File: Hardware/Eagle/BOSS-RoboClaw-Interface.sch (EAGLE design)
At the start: 10 parts, among them IC1 ISO7221AQDRQ1, J1 MOLEX 22112024, J2 MOLEX 22122034, J3 Amphenol 75869-130LF, J5 SAMTEC ESQ-110-33-T-D, J6 SAMTEC-ESQ-105-33-T-S, X1 Amphenol L77SDAH15SOL2RM8C309

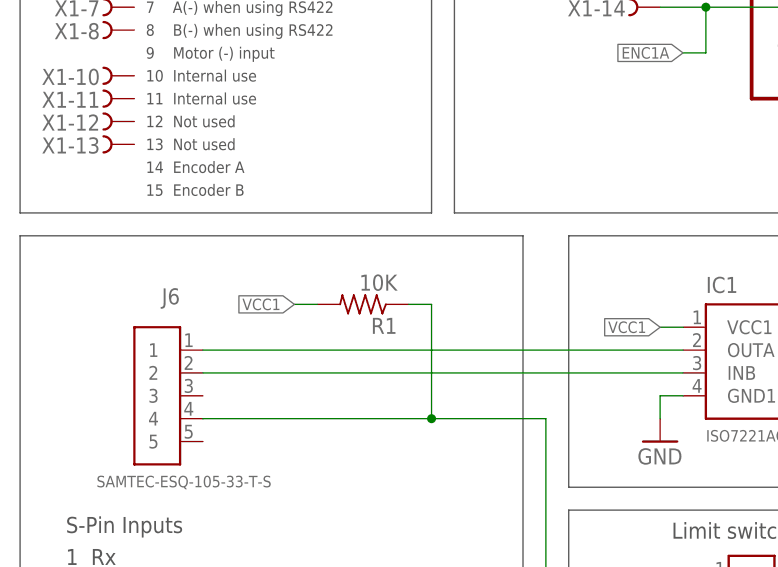
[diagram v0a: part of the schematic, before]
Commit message: Changed limit switch pullup to 4.7K
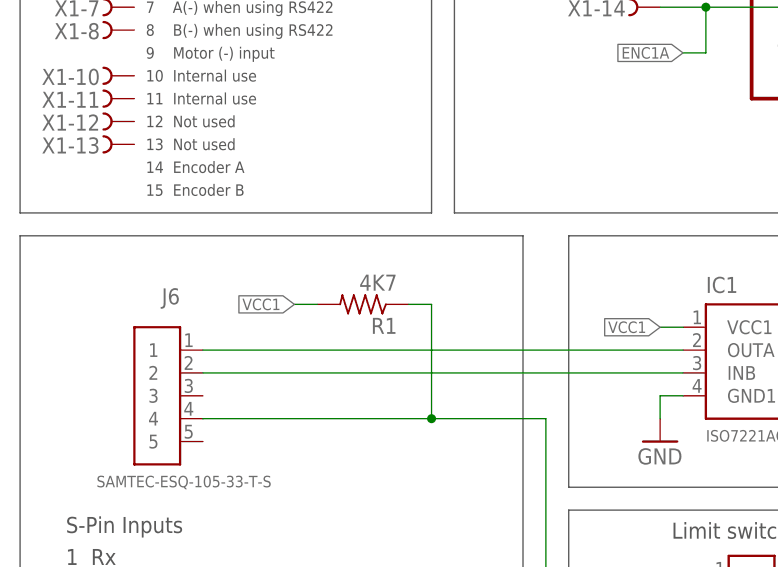
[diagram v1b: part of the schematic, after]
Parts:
- R1: value 10K -> 4K7
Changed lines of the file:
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@@
 <setting verticaltext="up"/>
 </settings>
-<grid distance="0.1" unitdist="inch" unit="inch" style="lines" multiple="1" display="yes" altdistance="0.01" altunitdist="inch" altunit="inch"/>
+<grid distance="0.1" unitdist="inch" unit="inch" style="lines" multiple="1" display="no" altdistance="0.01" altunitdist="inch" altunit="inch"/>
 <layers>
 <layer number="1" name="Top" color="4" fill="1" visible="no" active="no"/>
@@
 <part name="J6" library="AUmlib" library_urn="urn:adsk.eagle:library:9166017" deviceset="PINHD-1X5-ESQ-105-33-T-S" device="" package3d_urn="urn:adsk.eagle:package:24929591/4" value="SAMTEC-ESQ-105-33-T-S"/>
 <part name="J5" library="AUmlib" library_urn="urn:adsk.eagle:library:9166017" deviceset="PINHD-2X10-ESQ-110-33-T-D" device="SAMTEC" package3d_urn="urn:adsk.eagle:package:24929474/2" value="SAMTEC ESQ-110-33-T-D"/>
-<part name="R1" library="AUmlib" library_urn="urn:adsk.eagle:library:9166017" deviceset="R-US_" device="R0805" package3d_urn="urn:adsk.eagle:package:4021199/4" value="10K"/>
+<part name="R1" library="AUmlib" library_urn="urn:adsk.eagle:library:9166017" deviceset="R-US_" device="R0805" package3d_urn="urn:adsk.eagle:package:4021199/4" value="4K7"/>
 </parts>
 <sheets>

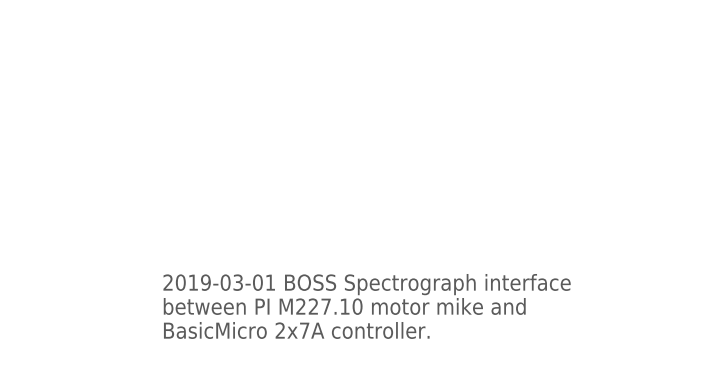
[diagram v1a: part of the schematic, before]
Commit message: Created a motor breakout board
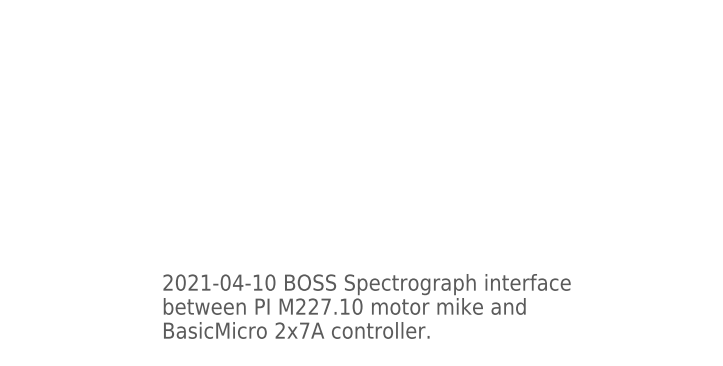
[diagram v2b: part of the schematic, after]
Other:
- note added: "2021-04-10 BOSS Spectrograph interface between PI M227.10 motor mike and BasicMicro 2x7A controller."
- note removed: "2019-03-01 BOSS Spectrograph interface between PI M227.10 motor mike and BasicMicro 2x7A controller."
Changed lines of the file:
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@@
 <wire x1="116.84" y1="129.54" x2="195.58" y2="129.54" width="0.1524" layer="97"/>
 <text x="172.72" y="170.18" size="1.778" layer="97" distance="100">Encoder Inputs</text>
-<text x="180.34" y="25.4" size="1.778" layer="97">2019-03-01 BOSS Spectrograph interface
+<text x="180.34" y="25.4" size="1.778" layer="97">2021-04-10 BOSS Spectrograph interface
 between PI M227.10 motor mike and
 BasicMicro 2x7A controller.</text>

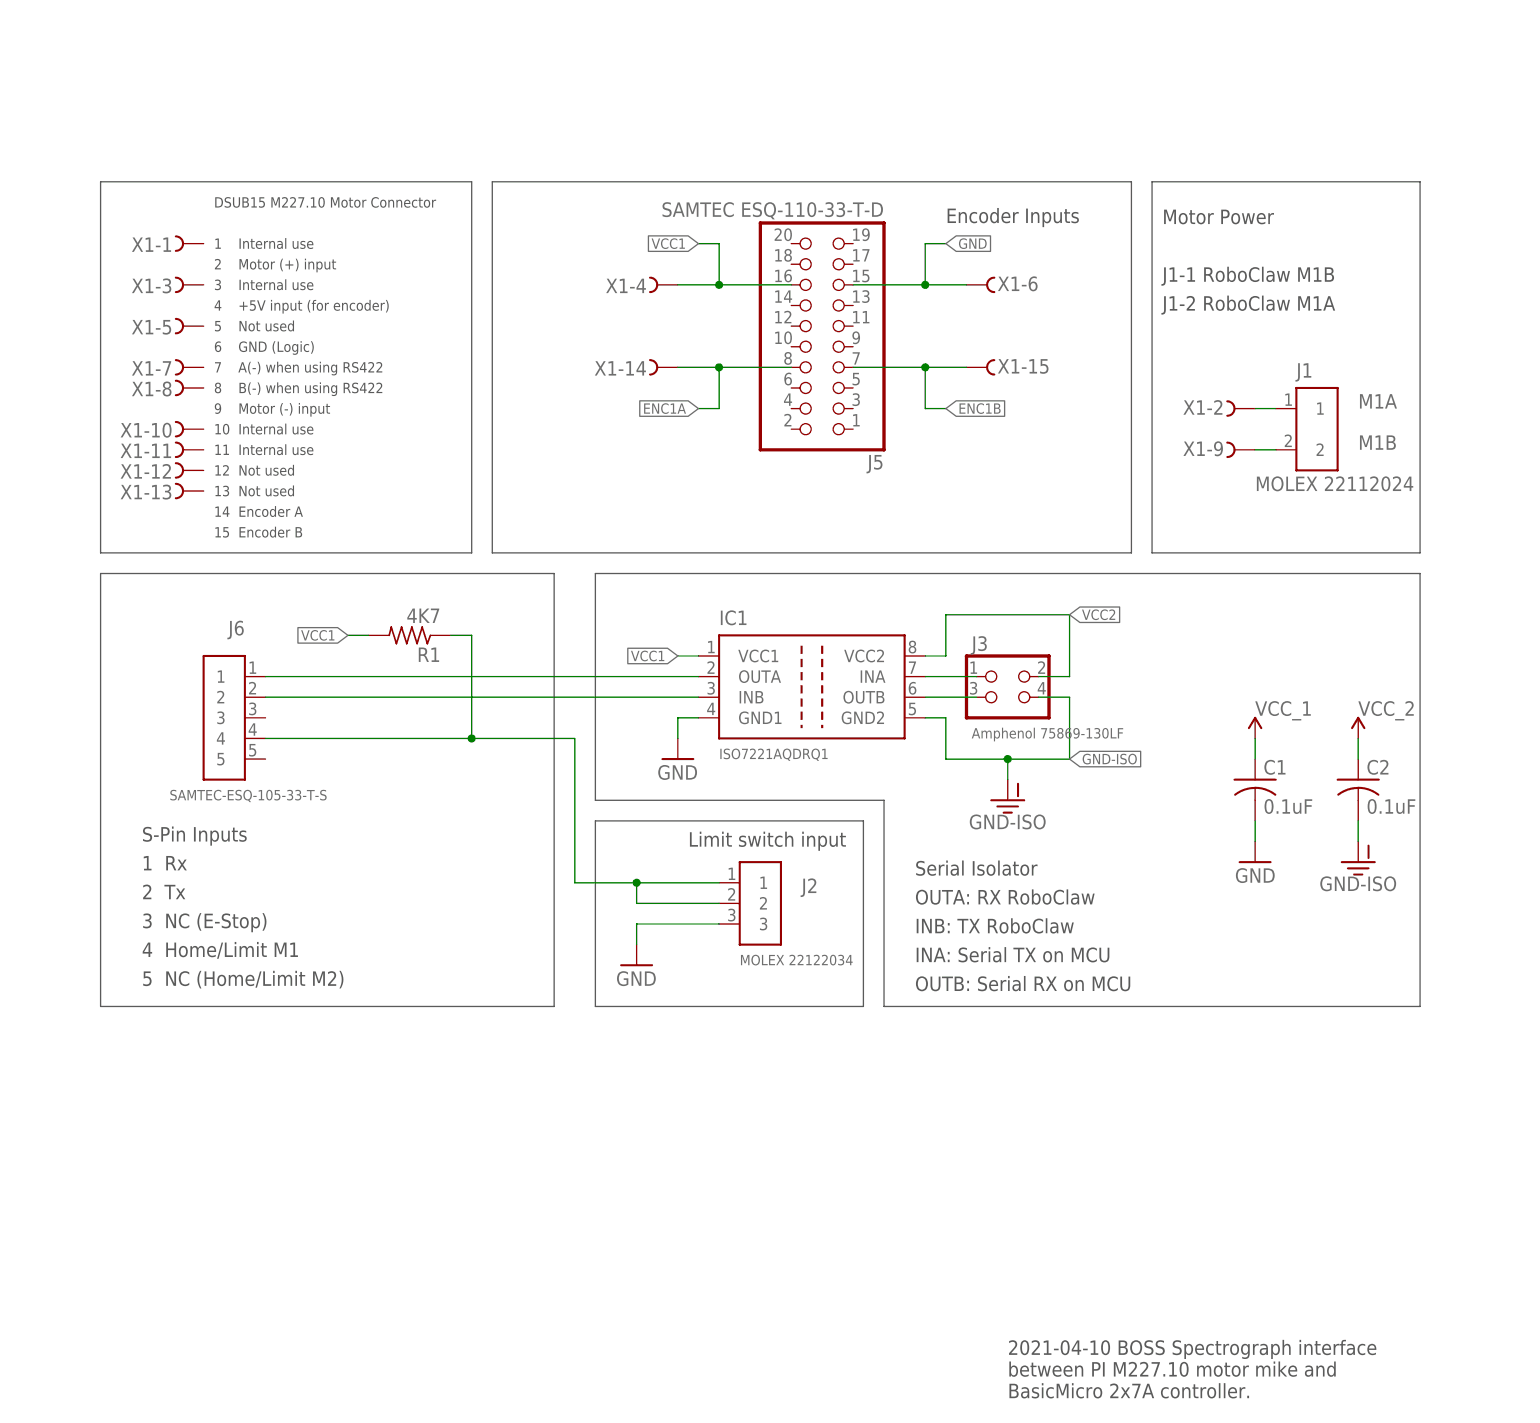
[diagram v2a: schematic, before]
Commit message: Includes open drain buffer
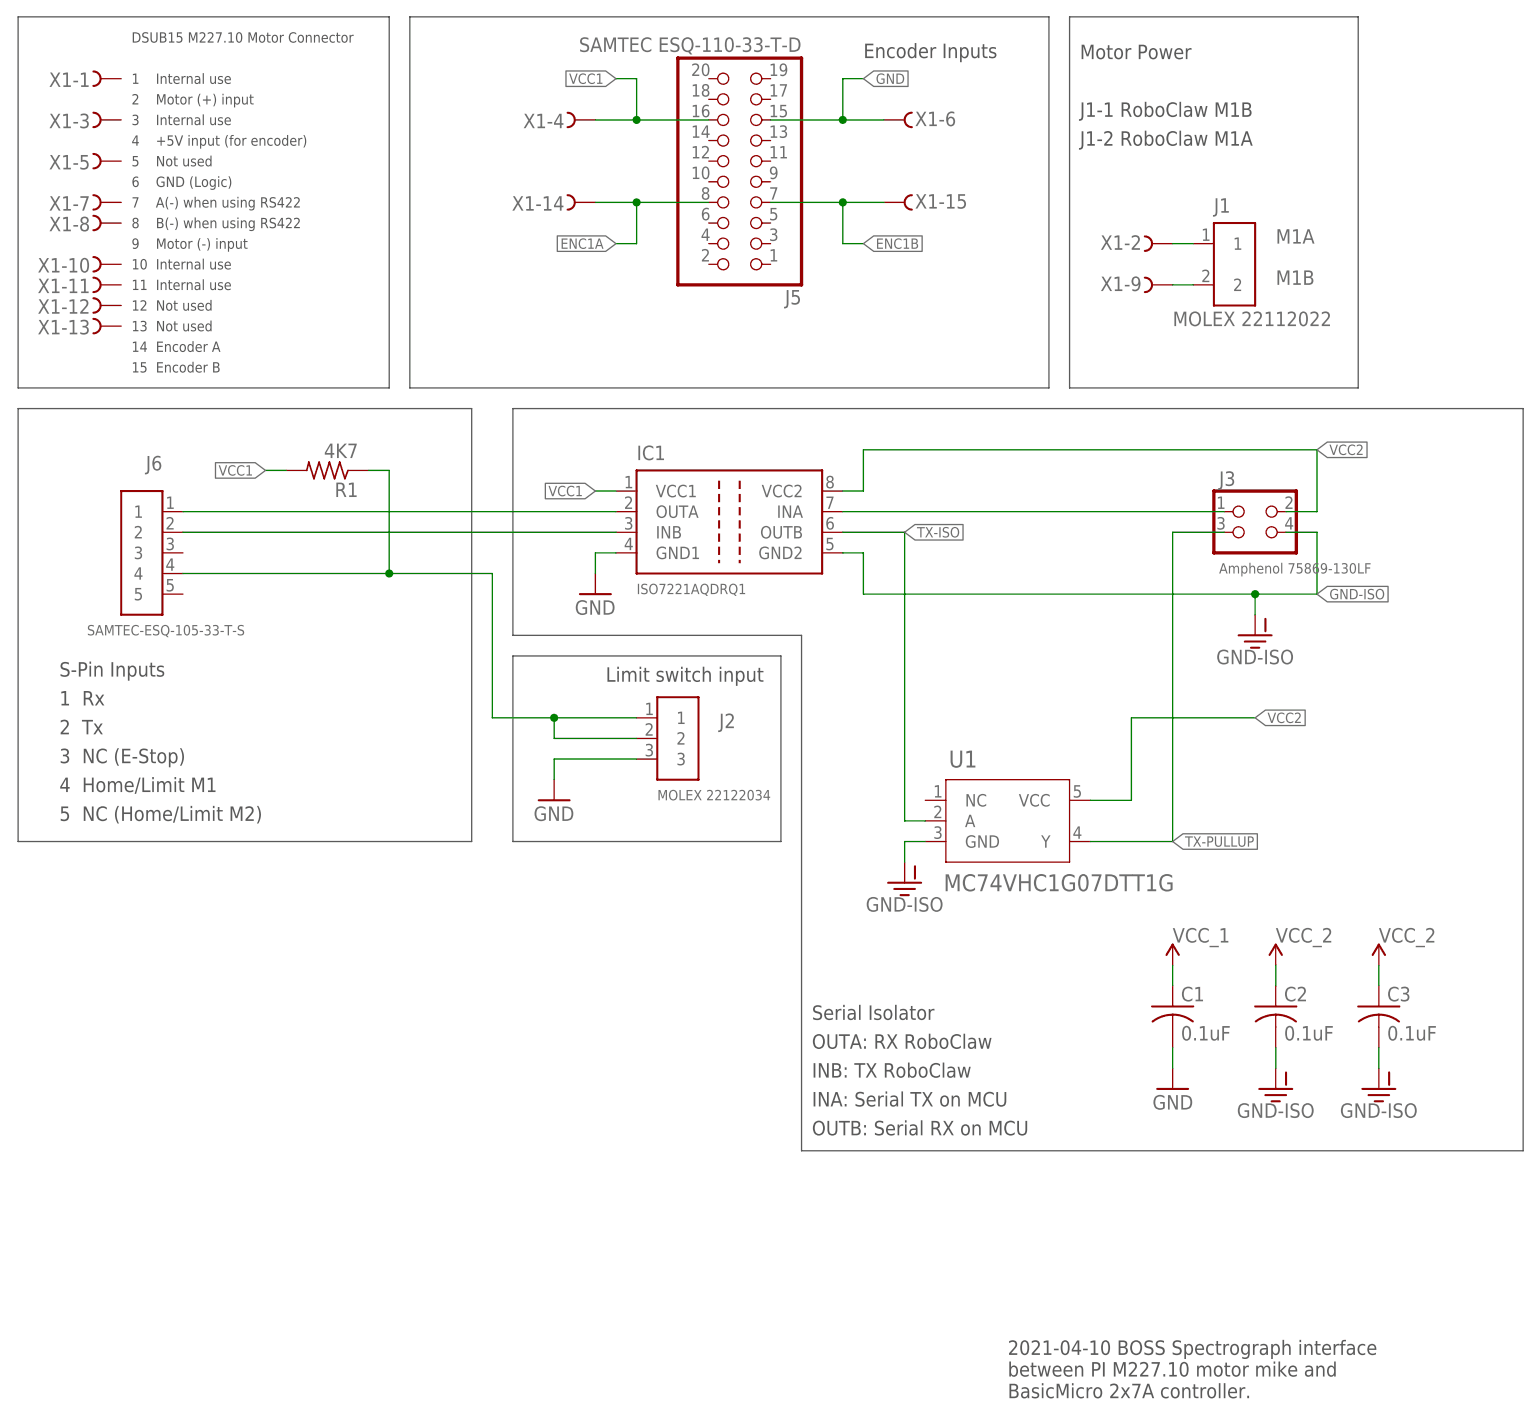
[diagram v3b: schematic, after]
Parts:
- added C3: 0.1uF, AUmlib:C-USC0805
- added U1: MC74VHC1G07DTT1G, AUmlib:MC74VHC1G07DTT1GSOT23-5_ONS-M
- J1: value MOLEX 22112024 -> MOLEX 22112022
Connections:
- net ROBO0TX renamed ROBO-TX
- removed net TX: IC1.OUTB, J3.3
- new net TX-ISO: IC1.OUTB, U1.A
- new net TX-PULLUP: J3.3, U1.Y
- net GND-ISO: now also C3.2, U1.GND
- net VCC2: now also C3.1, U1.VCC
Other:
- moved on the sheet: C1, C2, IC1, J1, J2, J3, J5, J6, R1, X1-1, X1-10, X1-11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
